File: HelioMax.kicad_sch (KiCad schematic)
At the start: 55 parts, among them J2 Conn_01x07, J3 Conn_01x07, J4 Conn_01x07, J5 Conn_01x07, J8 Conn_01x07, J9 Conn_01x07, SW0:10 SW0:3, SW0:11 SW0:2, SW0:12 SW0:1, SW0:7 SW0:6, SW0:8 SW0:5, SW0:9 SW0:4, SW1:10 SW1:3, SW1:11 SW1:2, SW1:12 SW1:1, SW1:13 SW1:0, SW1:9 SW1:4, SW2:10 SW2:3, SW2:11 SW2:2, SW2:12 SW2:1, SW2:13 SW2:0, SW2:7 SW2:6, SW2:8 SW2:5, SW2:9 SW2:4, SW3:10 SW3:3, SW3:11 SW3:2, SW3:12 SW3:1, SW3:13 SW3:0, SW3:8 SW3:5, SW3:9 SW3:4, SW4:10 SW4:3, SW4:11 SW4:2, SW4:12 SW4:1, SW4:13 SW4:0, SW4:7 SW4:6, SW4:8 SW4:5, SW4:9 SW4:4, SW5:10 SW5:3, SW5:11 SW5:2, SW5:12 SW5:1, SW5:13 SW5:0, SW5:7 SW5:6, SW5:8 SW5:5, SW5:9 SW5:4, SW6:10 SW6:3, SW6:11 SW6:2, SW6:12 SW6:1, SW6:13 SW6:0, SW6:7 SW6:6, SW6:8 SW6:5, SW6:9 SW6:4

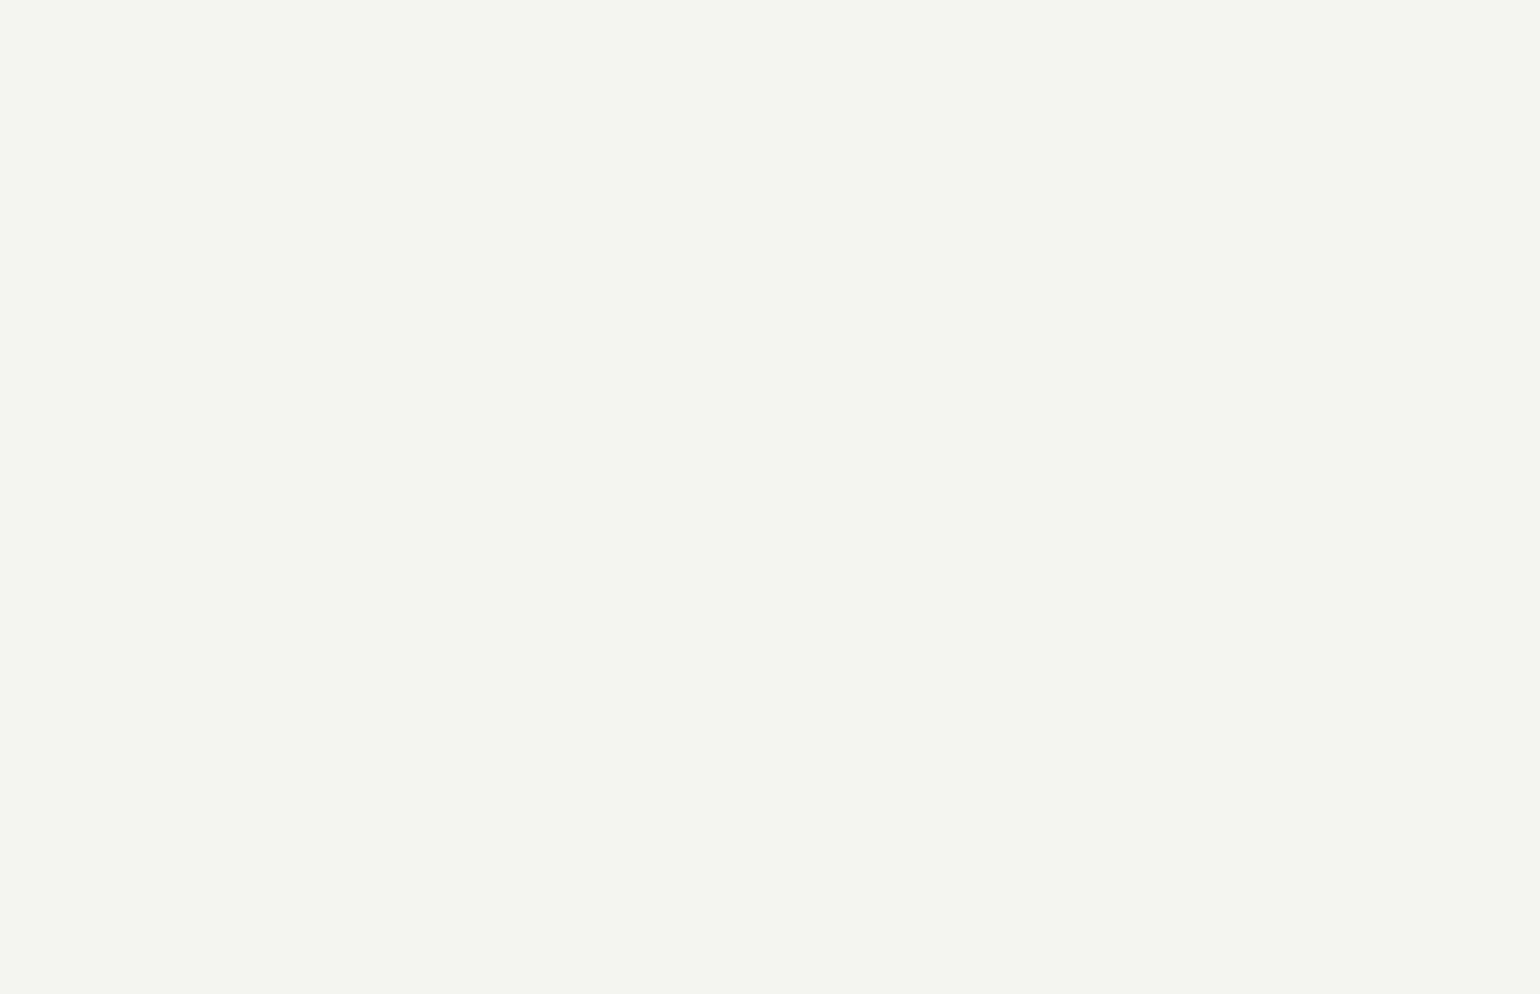
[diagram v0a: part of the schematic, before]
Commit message: Fixed edge cuts. Lots of DRC errors.
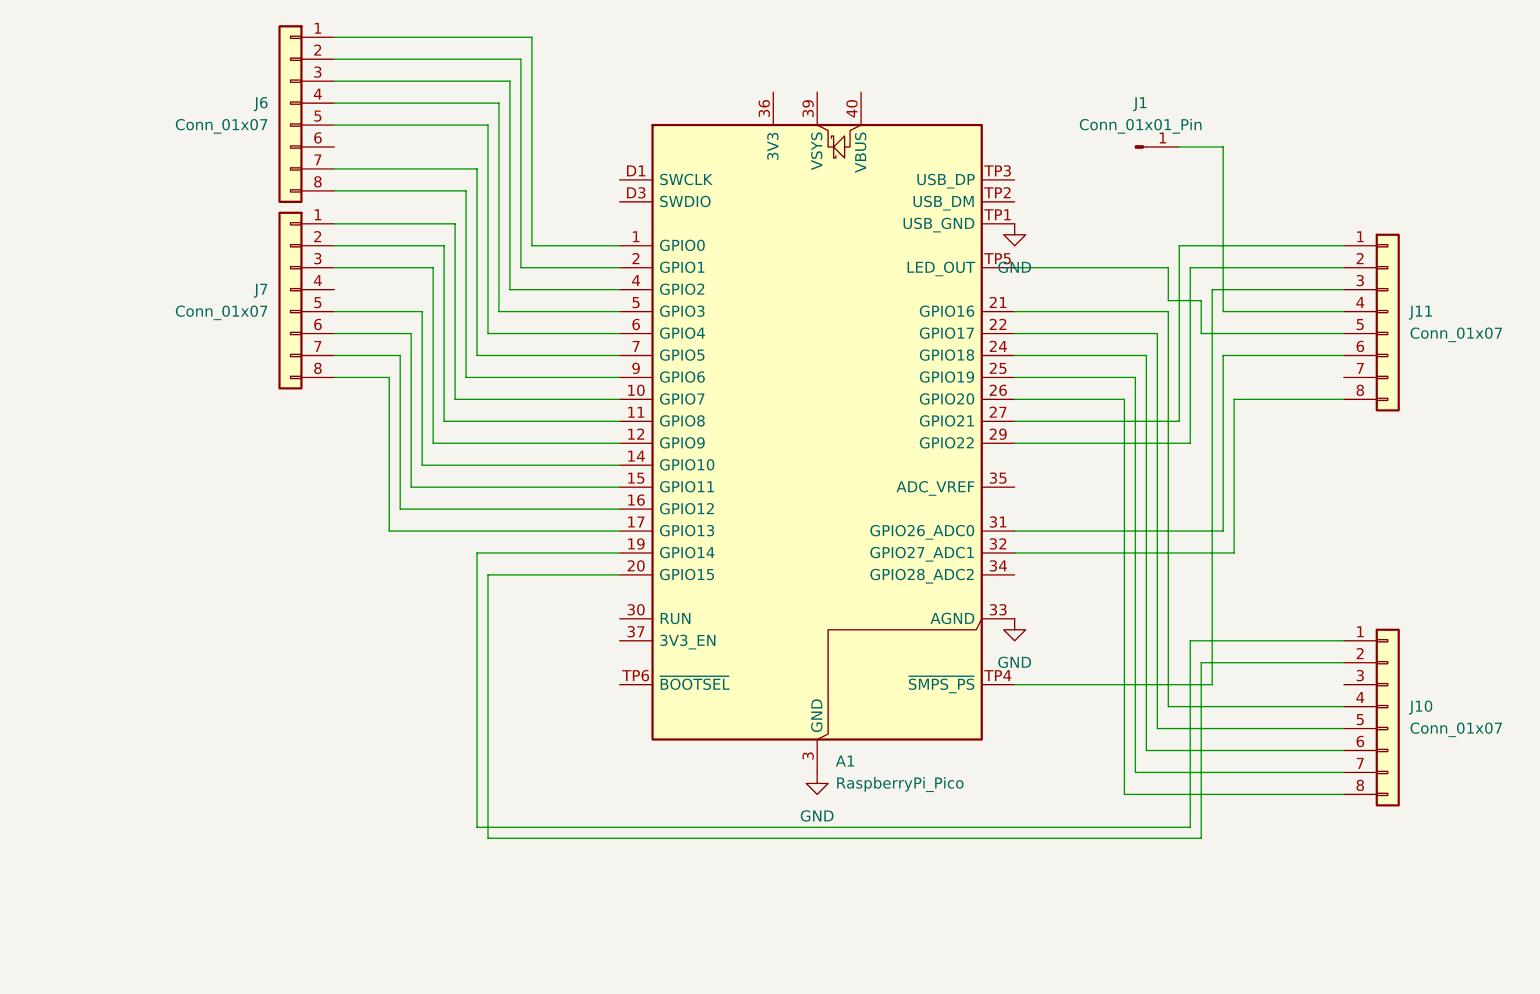
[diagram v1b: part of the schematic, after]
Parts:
- added A1: RaspberryPi_Pico, Module_RaspberryPi_Pico:RaspberryPi_Pico_Original_SMD_MountingHoles_HandSolder_Castellated, symbol MCU_Module_RaspberryPi_Pico:RaspberryPi_Pico_SecondaryPins
- added J1: Conn_01x01_Pin, Connector_PinHeader_1.00mm:PinHeader_1x01_P1.00mm_Vertical, symbol Connector:Conn_01x01_Pin
- added J10, J11, J6, J7: Conn_01x07, Connector_JST:JST_SH_SM08B-SRSS-TB_1x08-1MP_P1.00mm_Horizontal, symbol Connector_Generic:Conn_01x08
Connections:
- net GND: now also A1.13 (GND), A1.18 (GND), A1.23 (GND), A1.28 (GND), A1.3 (GND), A1.33 (AGND), A1.38 (GND), A1.8 (GND), A1.D2 (GND), A1.TP1 (USB_GND)
- new net: J1.1 (Pin_1), J11.4 (Pin_4)
- new net: A1.1 (GPIO0), J6.1 (Pin_1)
- new net: A1.2 (GPIO1), J6.2 (Pin_2)
- new net: A1.4 (GPIO2), J6.3 (Pin_3)
- new net: A1.5 (GPIO3), J6.4 (Pin_4)
- new net: A1.6 (GPIO4), J6.5 (Pin_5)
- new net: A1.7 (GPIO5), J6.7 (Pin_7)
- new net: A1.9 (GPIO6), J6.8 (Pin_8)
- new net: A1.10 (GPIO7), J7.1 (Pin_1)
- new net: A1.11 (GPIO8), J7.2 (Pin_2)
- new net: A1.12 (GPIO9), J7.3 (Pin_3)
- new net: A1.14 (GPIO10), J7.5 (Pin_5)
- new net: A1.15 (GPIO11), J7.6 (Pin_6)
- new net: A1.16 (GPIO12), J7.7 (Pin_7)
- new net: A1.17 (GPIO13), J7.8 (Pin_8)
- new net: A1.19 (GPIO14), J10.1 (Pin_1)
- new net: A1.20 (GPIO15), J10.2 (Pin_2)
- new net: A1.21 (GPIO16), J10.4 (Pin_4)
- new net: A1.22 (GPIO17), J10.5 (Pin_5)
- new net: A1.24 (GPIO18), J10.6 (Pin_6)
- new net: A1.25 (GPIO19), J10.7 (Pin_7)
- new net: A1.26 (GPIO20), J10.8 (Pin_8)
- new net: A1.27 (GPIO21), J11.1 (Pin_1)
- new net: A1.29 (GPIO22), J11.2 (Pin_2)
- new net: A1.31 (GPIO26_ADC0), J11.6 (Pin_6)
- new net: A1.32 (GPIO27_ADC1), J11.8 (Pin_8)
- new net: A1.TP4 (~{SMPS_PS}), J11.3 (Pin_3)
- new net: A1.TP5 (LED_OUT), J11.5 (Pin_5)

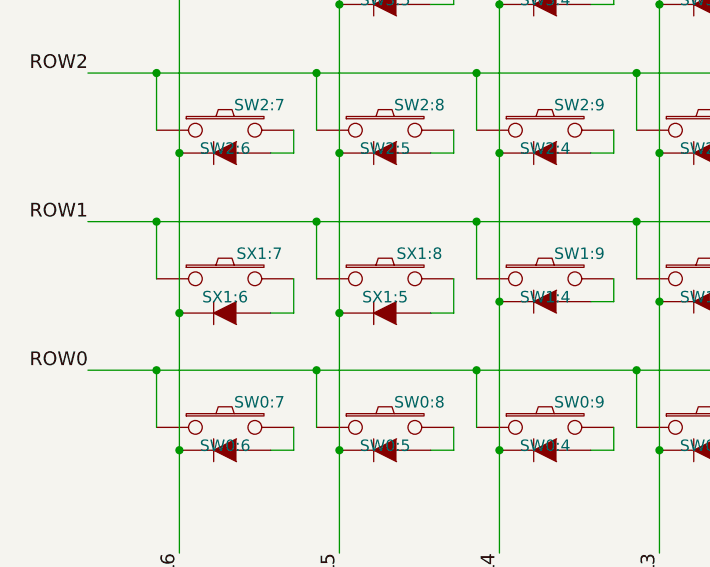
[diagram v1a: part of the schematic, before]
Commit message: Updated switch footprint and fixed all wiring.
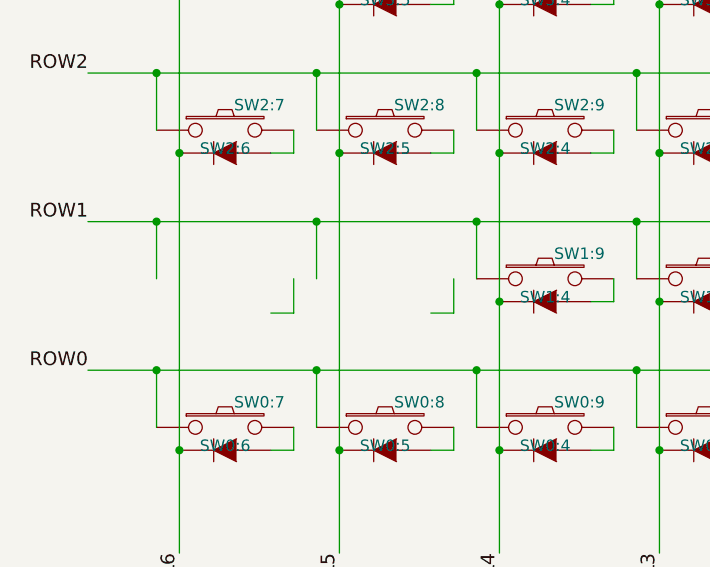
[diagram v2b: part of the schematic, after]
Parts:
- removed D1:7, D1:8: D, symbol ErgoDOX-rescue:DIODE
- removed SX1:7: SX1:6, symbol ErgoDOX-rescue:SWITCH_PUSH
- removed SX1:8: SX1:5, symbol ErgoDOX-rescue:SWITCH_PUSH
- SW0:10, SW0:11, SW0:12, SW0:7, SW0:8, SW0:9, SW1:10, SW1:11, SW1:12, SW1:13, SW1:9, SW2:10, SW2:11, SW2:12, SW2:13, SW2:7, SW2:8, SW2:9, SW3:10, SW3:11, SW3:12, SW3:13, SW3:8, SW3:9, SW4:10, SW4:11, SW4:12, SW4:13, SW4:7, SW4:8, SW4:9, SW5:10, SW5:11, SW5:12, SW5:13, SW5:7, SW5:8, SW5:9, SW6:10, SW6:11, SW6:12, SW6:13, SW6:7, SW6:8, SW6:9: footprint ErgoDOX pcb:MX_FLIP_DIODE -> ErgoDOX pcb:MX_FLIP_CLEAN

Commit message: Replace relic holes, include fonts, general clean-up and rewiring.
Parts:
- added H1, H10, H11, H12, H13, H14, H15, H2, H3, H4, H5, H6, H7, H8, H9: MountingHole, MountingHole:MountingHole_3.2mm_M3, symbol Mechanical:MountingHole

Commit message: Added donations (as if anybody will do that)
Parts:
- removed H15: MountingHole, MountingHole:MountingHole_3.2mm_M3, symbol Mechanical:MountingHole
- J2: value Conn_01x07 -> Conn_to_Pollex_Cluster
- J3: value Conn_01x07 -> Conn_Pollex_Cluster
- J4: value Conn_01x07 -> Conn_C_to_Praetor_Enclave
- J5: value Conn_01x07 -> Conn_R_to_Praetor_Enclave
- J8: value Conn_01x07 -> Conn_to_Telorum_Belt
- J9: value Conn_01x07 -> Conn_Telorum_Belt
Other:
- moved on the sheet: A1, H1, H10, H11, H12, H13, H14, H2, H3, H4, H5, H6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
